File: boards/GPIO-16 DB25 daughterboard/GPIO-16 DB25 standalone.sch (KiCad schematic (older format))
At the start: 13 parts, among them J201 DB9, J202 DB9, U201 ISL83387E, U202 24AA014

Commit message: Added bypass capacitor to EEPROM in GPIO16 DB25 dboard and cleaned template
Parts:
- removed C201, C202, C203, C204, C205, C206: 0.1u, ~, symbol CSMALL
- removed D201: LED, ~, symbol LED
- removed J201, J202: DB9, symbol DB9
- removed R201: R, ~, symbol R
- removed U201: ISL83387E, ~, symbol ISL83387E
- added C?: 0.1u, ~, symbol CSMALL
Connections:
- net labels removed: A_CTS, A_DSR, A_DTR, A_RTS, A_RX, A_TX, B_CTS, B_DSR, B_DTR, B_RTS, B_RX, B_TX, CTS_ISO, C_CTS, C_DSR, C_DTR, C_RTS, C_RX, C_TX, DSR_ISO, DTR_ISO, RTS_ISO, RX_ISO, TX_ISO, VCC_5V_ISO
- wire segments 90 -> 19
- no-connect marks 4 -> 0
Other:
- moved on the sheet: R203

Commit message: GPIO16 DB25 Daughterboard done
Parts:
- added J201: DB25, symbol DB25
- gave numbers to parts that had none: 1
- renumbered R203 to R201, U202 to U201
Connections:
- net labels added: CTS_ISO_A, CTS_ISO_B, DSR_ISO_A, DSR_ISO_B, DTR_ISO_A, DTR_ISO_B, GPIO0, GPIO1, GPIO10, GPIO11, GPIO12, GPIO13, GPIO14, GPIO15, GPIO2, GPIO3, GPIO4, GPIO5, GPIO6, GPIO7, GPIO8, GPIO9, RTS_ISO_A, RTS_ISO_B, RX_ISO_A, RX_ISO_B, TX_ISO_A, TX_ISO_B, VCC_5V_ISO
- wire segments 19 -> 73
- no-connect marks 0 -> 15
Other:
- note removed: "DTE Serial DB9 pinout:\n1 DCD <-- Data Carrier Detect\n2 RXD <-- Receive Data\n3 TXD --> Transmit Data\n4 DTR --> Data Terminal Ready\n5 GND --- System Ground\n6 DSR <-- Data Set Ready\n7 RTS --> Request to Send\n8 CTS <-- Clear to Send\n9 RI <-- Ring Indicator"

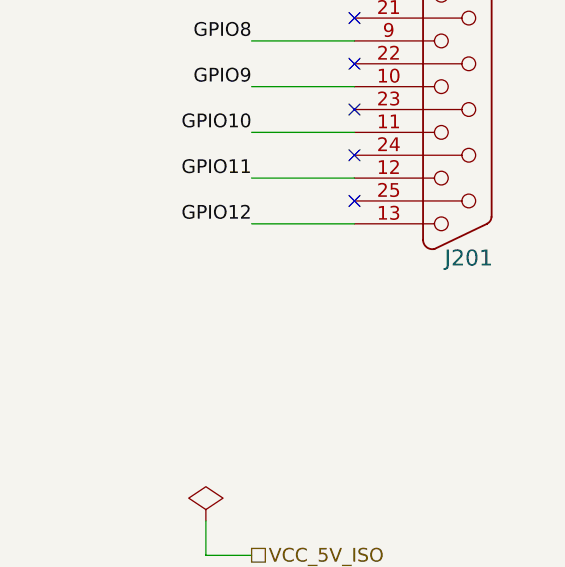
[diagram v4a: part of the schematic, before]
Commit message: Added DB25 pinout note to GPIO16 DB25 Daughterboard
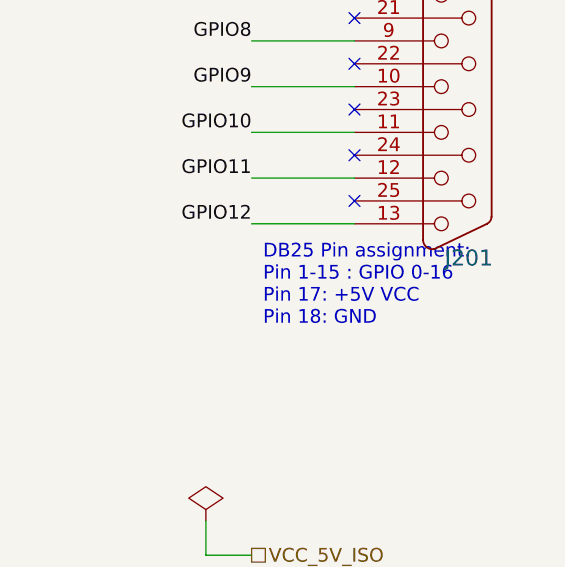
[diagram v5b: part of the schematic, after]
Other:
- note added: "DB25 Pin assignment:\nPin 1-15 : GPIO 0-16\nPin 17: +5V VCC\nPin 18: GND"
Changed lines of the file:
@@
 Text HLabel 6850 3250 0    60   UnSpc ~ 0
 GND_ISO
+Text Notes 7300 5200 0    60   ~ 0
+DB25 Pin assignment:\nPin 1-15 : GPIO 0-16\nPin 17: +5V VCC\nPin 18: GND
 $EndSCHEMATC
